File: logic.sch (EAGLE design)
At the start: 7 parts, among them CON1 PINHEAD_1X10-2, CON2 PINHEAD_1X10-2, CON3 PINHEAD_1X06-2, CON4 PINHEAD_1X02-2, CON5 PINHEAD_1X02-2, CON6 PINHEAD_1X02-2

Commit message: Routing is complete again. Now with BEC output
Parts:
- removed CON3: PINHEAD_1X06-2, pinhead:PINHEAD_1X06-2
- added CON7: PINHEAD_1X07-2, pinhead:PINHEAD_1X07-2
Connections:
- new net BEC_ENABLE: CON7.4, MODULE2.BEC_ENABLE_OUT
- net ADJ: now also CON7.2; no longer CON3.2
- net BLUE: now also CON7.1; no longer CON3.1
- net CAN1_LED: now also CON7.7; no longer CON3.6
- net CAN1_RX: now also CON7.5; no longer CON3.4
- net CAN1_TX: now also CON7.6; no longer CON3.5
- net GPIO1: now also CON7.3; no longer CON3.3
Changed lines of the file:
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@@
 <part name="CON4" library="pinhead" library_urn="urn:adsk.eagle:library:2540341" deviceset="PINHEAD_1X02" device="-2" package3d_urn="urn:adsk.eagle:package:6503394/3"/>
 <part name="CON5" library="pinhead" library_urn="urn:adsk.eagle:library:2540341" deviceset="PINHEAD_1X02" device="-2" package3d_urn="urn:adsk.eagle:package:6503394/3"/>
-<part name="CON3" library="pinhead" library_urn="urn:adsk.eagle:library:2540341" deviceset="PINHEAD_1X06" device="-2" package3d_urn="urn:adsk.eagle:package:6650269/2"/>
 <part name="CON6" library="pinhead" library_urn="urn:adsk.eagle:library:2540341" deviceset="PINHEAD_1X02" device="-2" package3d_urn="urn:adsk.eagle:package:6503394/3"/>
 <part name="GND2" library="supply_symbols" library_urn="urn:adsk.eagle:library:5017758" deviceset="GND" device="" value="GND"/>
 <part name="GND3" library="supply_symbols" library_urn="urn:adsk.eagle:library:5017758" deviceset="GND" device="" value="GND"/>
 <part name="+P3" library="supply_symbols" library_urn="urn:adsk.eagle:library:5017758" deviceset="5V" device=""/>
+<part name="CON7" library="pinhead" library_urn="urn:adsk.eagle:library:2540341" deviceset="PINHEAD_1X07" device="-2" package3d_urn="urn:adsk.eagle:package:2540391/3"/>
 </parts>
 <sheets>
@@
 <attribute name="NAME" x="226.06" y="87.63" size="1.778" layer="95" font="vector" ratio="15" rot="MR180" align="center"/>
 </instance>
-<instance part="CON3" gate="G$1" x="223.52" y="114.3" smashed="yes">
-<attribute name="NAME" x="226.06" y="133.35" size="1.778" layer="95" font="vector" ratio="15" align="center"/>
-</instance>
 <instance part="CON6" gate="G$1" x="223.52" y="162.56" smashed="yes" rot="MR180">
 <attribute name="NAME" x="226.06" y="153.67" size="1.778" layer="95" font="vector" ratio="15" rot="MR180" align="center"/>
@@
 <instance part="+P3" gate="G$1" x="233.68" y="96.52" smashed="yes">
 <attribute name="VALUE" x="233.68" y="100.076" size="1.27" layer="96" font="vector" ratio="15" align="center"/>
+</instance>
+<instance part="CON7" gate="G$1" x="223.52" y="114.3" smashed="yes">
+<attribute name="NAME" x="226.06" y="135.89" size="1.778" layer="95" font="vector" ratio="15" align="center"/>
 </instance>
 </instances>
@@
 </segment>
 <segment>
-<pinref part="CON3" gate="G$1" pin="5"/>
-<wire x1="231.14" y1="127" x2="233.68" y2="127" width="0.1524" layer="91"/>
-<label x="233.68" y="127" size="1.27" layer="95" xref="yes"/>
+<wire x1="231.14" y1="129.54" x2="233.68" y2="129.54" width="0.1524" layer="91"/>
+<label x="233.68" y="129.54" size="1.27" layer="95" xref="yes"/>
+<pinref part="CON7" gate="G$1" pin="6"/>
 </segment>
 </net>
@@
 </segment>
 <segment>
-<pinref part="CON3" gate="G$1" pin="4"/>
-<wire x1="231.14" y1="124.46" x2="233.68" y2="124.46" width="0.1524" layer="91"/>
-<label x="233.68" y="124.46" size="1.27" layer="95" xref="yes"/>
+<wire x1="231.14" y1="127" x2="233.68" y2="127" width="0.1524" layer="91"/>
+<label x="233.68" y="127" size="1.27" layer="95" xref="yes"/>
+<pinref part="CON7" gate="G$1" pin="5"/>
 </segment>
 </net>
@@
 </segment>
 <segment>
-<pinref part="CON3" gate="G$1" pin="2"/>
 <wire x1="231.14" y1="119.38" x2="233.68" y2="119.38" width="0.1524" layer="91"/>
 <label x="233.68" y="119.38" size="1.27" layer="95" xref="yes"/>
+<pinref part="CON7" gate="G$1" pin="2"/>
 </segment>
 </net>
@@
 </segment>
 <segment>
-<pinref part="CON3" gate="G$1" pin="3"/>
 <wire x1="231.14" y1="121.92" x2="233.68" y2="121.92" width="0.1524" layer="91"/>
 <label x="233.68" y="121.92" size="1.27" layer="95" xref="yes"/>
+<pinref part="CON7" gate="G$1" pin="3"/>
 </segment>
 </net>
@@
 </segment>
 <segment>
-<pinref part="CON3" gate="G$1" pin="6"/>
-<wire x1="231.14" y1="129.54" x2="233.68" y2="129.54" width="0.1524" layer="91"/>
-<label x="233.68" y="129.54" size="1.27" layer="95" xref="yes"/>
+<pinref part="CON7" gate="G$1" pin="7"/>
+<wire x1="231.14" y1="132.08" x2="233.68" y2="132.08" width="0.1524" layer="91"/>
+<label x="233.68" y="132.08" size="1.27" layer="95" xref="yes"/>
 </segment>
 </net>
@@
 </segment>
 <segment>
-<pinref part="CON3" gate="G$1" pin="1"/>
 <wire x1="231.14" y1="116.84" x2="233.68" y2="116.84" width="0.1524" layer="91"/>
 <label x="233.68" y="116.84" size="1.27" layer="95" xref="yes"/>
+<pinref part="CON7" gate="G$1" pin="1"/>
 </segment>
 </net>
@@
 </segment>
 </net>
+<net name="BEC_ENABLE" class="0">
+<segment>
+<wire x1="231.14" y1="124.46" x2="233.68" y2="124.46" width="0.1524" layer="91"/>
+<label x="233.68" y="124.46" size="1.27" layer="95" xref="yes"/>
+<pinref part="CON7" gate="G$1" pin="4"/>
+</segment>
+<segment>
+<pinref part="MODULE2" gate="G$1" pin="BEC_ENABLE_OUT"/>
+<wire x1="165.1" y1="99.06" x2="167.64" y2="99.06" width="0.1524" layer="91"/>
+<label x="167.64" y="99.06" size="1.27" layer="95" xref="yes"/>
+</segment>
+</net>

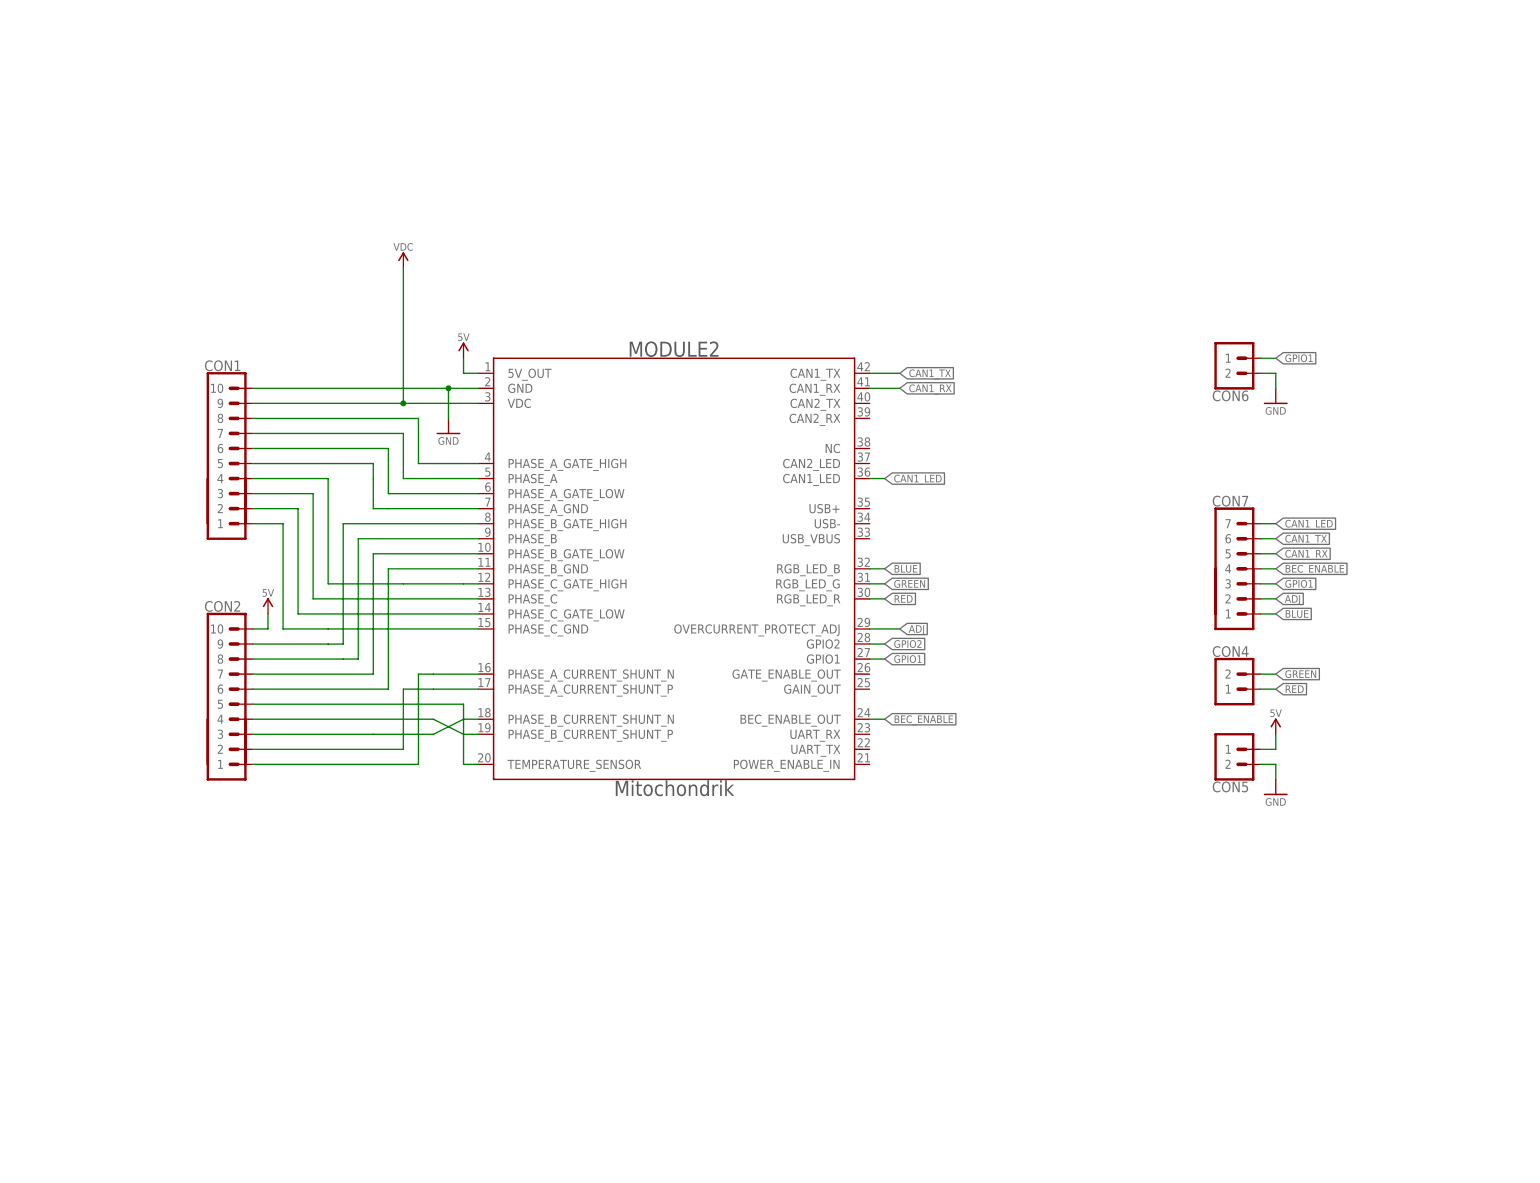
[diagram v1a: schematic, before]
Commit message: pinout fixes
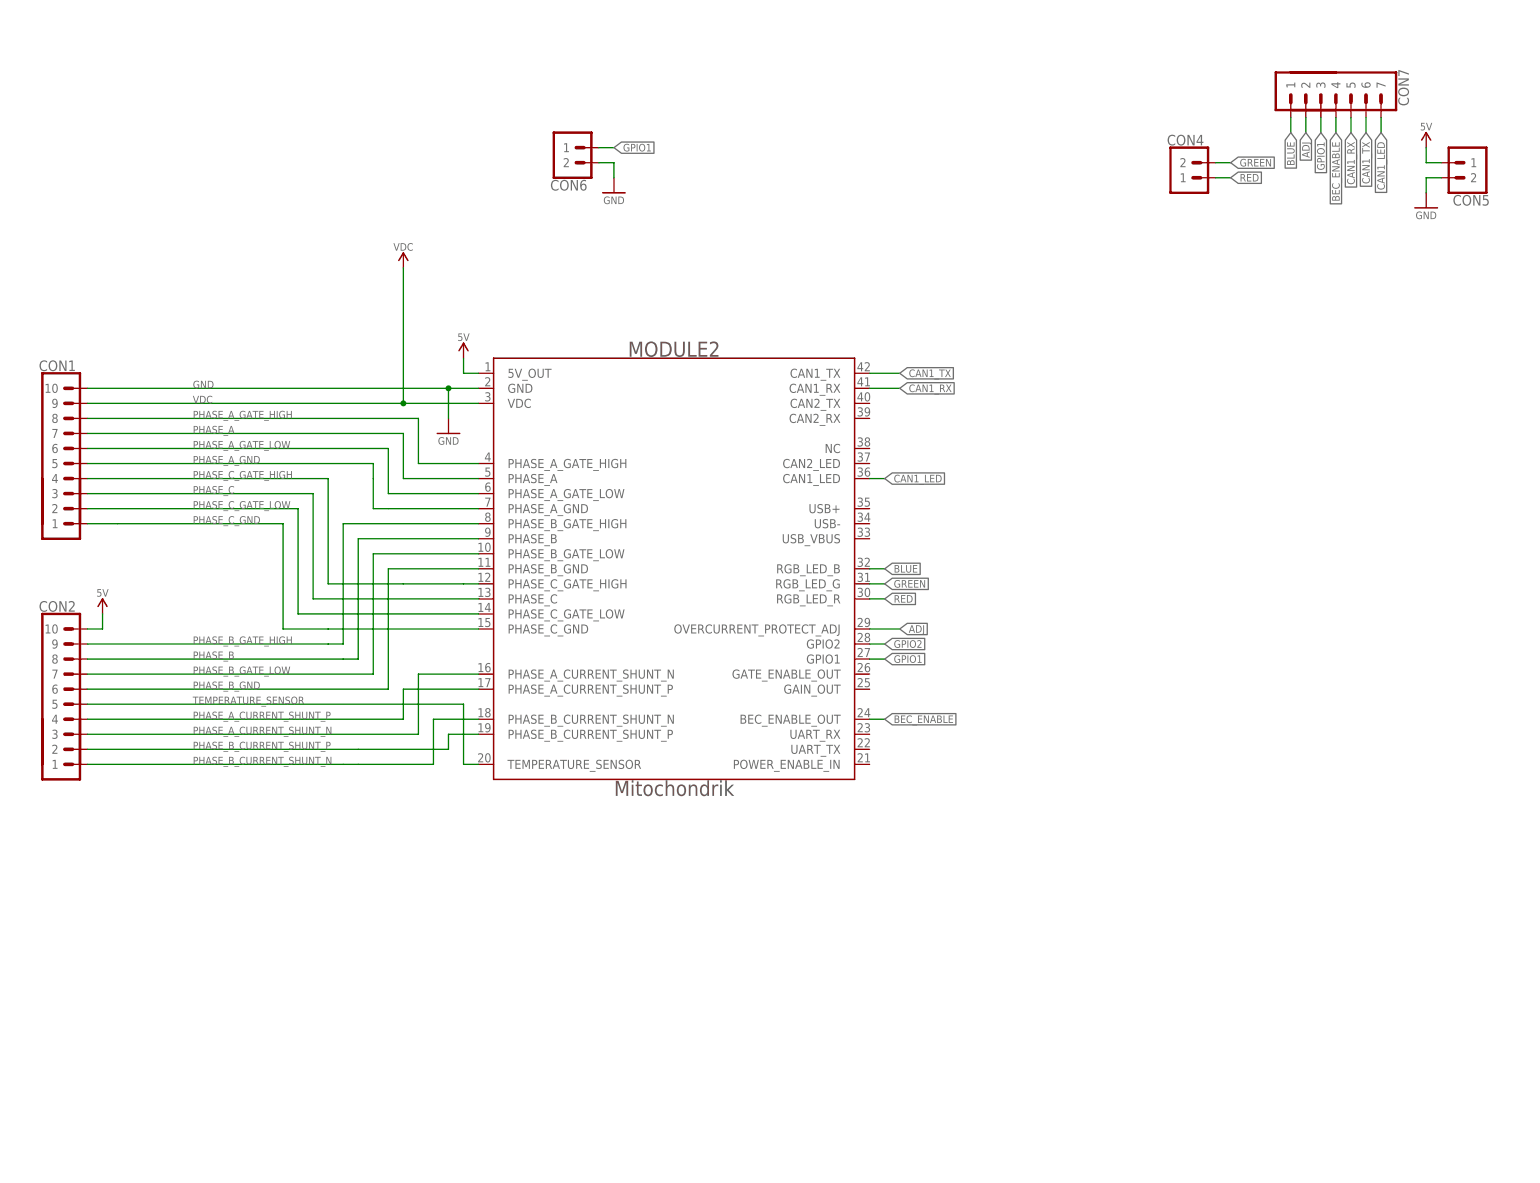
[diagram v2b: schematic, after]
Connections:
- removed net N$1: CON2.3, MODULE2.PHASE_B_CURRENT_SHUNT_N
- removed net N$2: CON2.2, MODULE2.PHASE_A_CURRENT_SHUNT_P
- removed net N$3: CON2.1, MODULE2.PHASE_A_CURRENT_SHUNT_N
- removed net N$4: CON2.4, MODULE2.PHASE_B_CURRENT_SHUNT_P
- removed net N$5: CON1.1, MODULE2.PHASE_C_GND
- new net PHASE_A_CURRENT_SHUNT_N: CON2.3, MODULE2.PHASE_A_CURRENT_SHUNT_N
- new net PHASE_A_CURRENT_SHUNT_P: CON2.4, MODULE2.PHASE_A_CURRENT_SHUNT_P
- new net PHASE_B_CURRENT_SHUNT_N: CON2.1, MODULE2.PHASE_B_CURRENT_SHUNT_N
- new net PHASE_B_CURRENT_SHUNT_P: CON2.2, MODULE2.PHASE_B_CURRENT_SHUNT_P
- new net PHASE_B_GND: CON2.6, MODULE2.PHASE_B_GND
- net PHASE_B: now also CON2.8, MODULE2.PHASE_B; no longer CON1.3, MODULE2.PHASE_C
- net PHASE_B_GATE_HIGH: now also CON2.9, MODULE2.PHASE_B_GATE_HIGH; no longer CON1.4, MODULE2.PHASE_C_GATE_HIGH
- net PHASE_B_GATE_LOW: now also CON2.7, MODULE2.PHASE_B_GATE_LOW; no longer CON1.2, MODULE2.PHASE_C_GATE_LOW
- net PHASE_C: now also CON1.3, MODULE2.PHASE_C; no longer CON2.8, MODULE2.PHASE_B
- net PHASE_C_GATE_HIGH: now also CON1.4, MODULE2.PHASE_C_GATE_HIGH; no longer CON2.9, MODULE2.PHASE_B_GATE_HIGH
- net PHASE_C_GATE_LOW: now also CON1.2, MODULE2.PHASE_C_GATE_LOW; no longer CON2.7, MODULE2.PHASE_B_GATE_LOW
- net PHASE_C_GND: now also CON1.1, MODULE2.PHASE_C_GND; no longer CON2.6, MODULE2.PHASE_B_GND
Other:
- moved on the sheet: CON1, CON2, CON4, CON5, CON6, CON7

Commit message: updates
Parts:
- renumbered MODULE2 to MODULE1

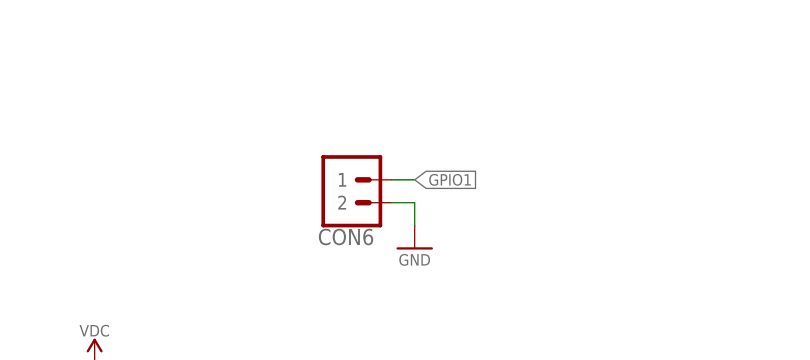
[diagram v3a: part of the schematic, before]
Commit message: Logic board update.
Thermistor connection moved to other side of the PCB
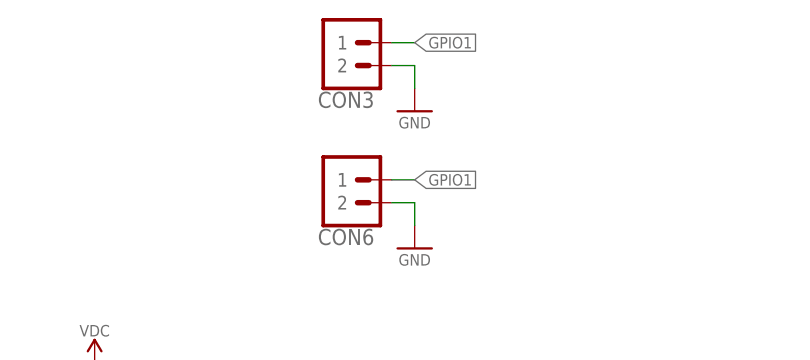
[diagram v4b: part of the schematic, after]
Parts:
- added CON3: PINHEAD_1X02-2, pinhead:PINHEAD_1X02-2
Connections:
- net GND: now also CON3.2
- net GPIO1: now also CON3.1
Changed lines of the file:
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@@
 </attributes>
 <variantdefs>
-<variantdef name="BASIC" current="yes"/>
+<variantdef name="BASIC"/>
 </variantdefs>
 <classes>
@@
 <part name="+P3" library="supply_symbols" library_urn="urn:adsk.eagle:library:5017758" deviceset="5V" device=""/>
 <part name="CON7" library="pinhead" library_urn="urn:adsk.eagle:library:2540341" deviceset="PINHEAD_1X07" device="-2" package3d_urn="urn:adsk.eagle:package:2540391/3"/>
+<part name="CON3" library="pinhead" library_urn="urn:adsk.eagle:library:2540341" deviceset="PINHEAD_1X02" device="-2" package3d_urn="urn:adsk.eagle:package:6503394/3">
+<variant name="BASIC" populate="no"/>
+</part>
+<part name="GND4" library="supply_symbols" library_urn="urn:adsk.eagle:library:5017758" deviceset="GND" device="" value="GND"/>
 </parts>
 <sheets>
@@
 <attribute name="NAME" x="255.27" y="205.74" size="1.778" layer="95" font="vector" ratio="15" rot="R270" align="center"/>
 </instance>
+<instance part="CON3" gate="G$1" x="111.76" y="213.36" smashed="yes" rot="MR180">
+<attribute name="NAME" x="114.3" y="204.47" size="1.778" layer="95" font="vector" ratio="15" rot="MR180" align="center"/>
+</instance>
+<instance part="GND4" gate="1" x="121.92" y="203.2" smashed="yes">
+<attribute name="VALUE" x="121.92" y="201.93" size="1.27" layer="96" font="vector" ratio="15" align="center"/>
+</instance>
 </instances>
 <busses>
@@
 <pinref part="CON5" gate="G$1" pin="2"/>
 <wire x1="259.08" y1="190.5" x2="261.62" y2="190.5" width="0.1524" layer="91"/>
+</segment>
+<segment>
+<pinref part="GND4" gate="1" pin="GND"/>
+<wire x1="121.92" y1="208.28" x2="121.92" y2="205.74" width="0.1524" layer="91"/>
+<pinref part="CON3" gate="G$1" pin="2"/>
+<wire x1="121.92" y1="208.28" x2="119.38" y2="208.28" width="0.1524" layer="91"/>
 </segment>
 </net>
@@
 <pinref part="CON7" gate="G$1" pin="3"/>
 </segment>
-</net>
+<segment>
+<pinref part="CON3" gate="G$1" pin="1"/>
+<wire x1="119.38" y1="210.82" x2="121.92" y2="210.82" width="0.1524" layer="91"/>
+<label x="121.92" y="210.82" size="1.27" layer="95" xref="yes"/>
+</segment>
+</net>
